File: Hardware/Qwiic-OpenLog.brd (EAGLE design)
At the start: 25.4 x 26.7 mm, 30 parts, among them J2 SMD, J3 PTH, J4 SMD, J5 ISP, Q1 16MHZ, U2 ATMEGA328P, U3 microSD Socket

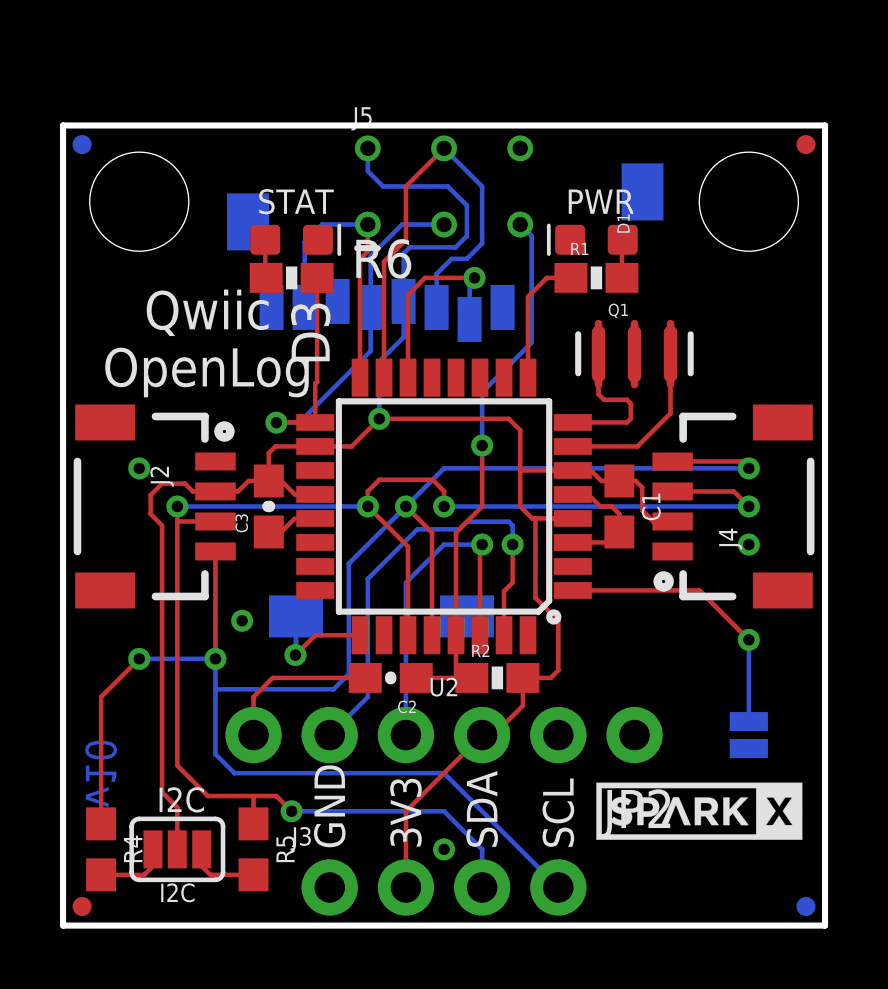
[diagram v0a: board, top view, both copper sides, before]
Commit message: Updating with Buzzard labels
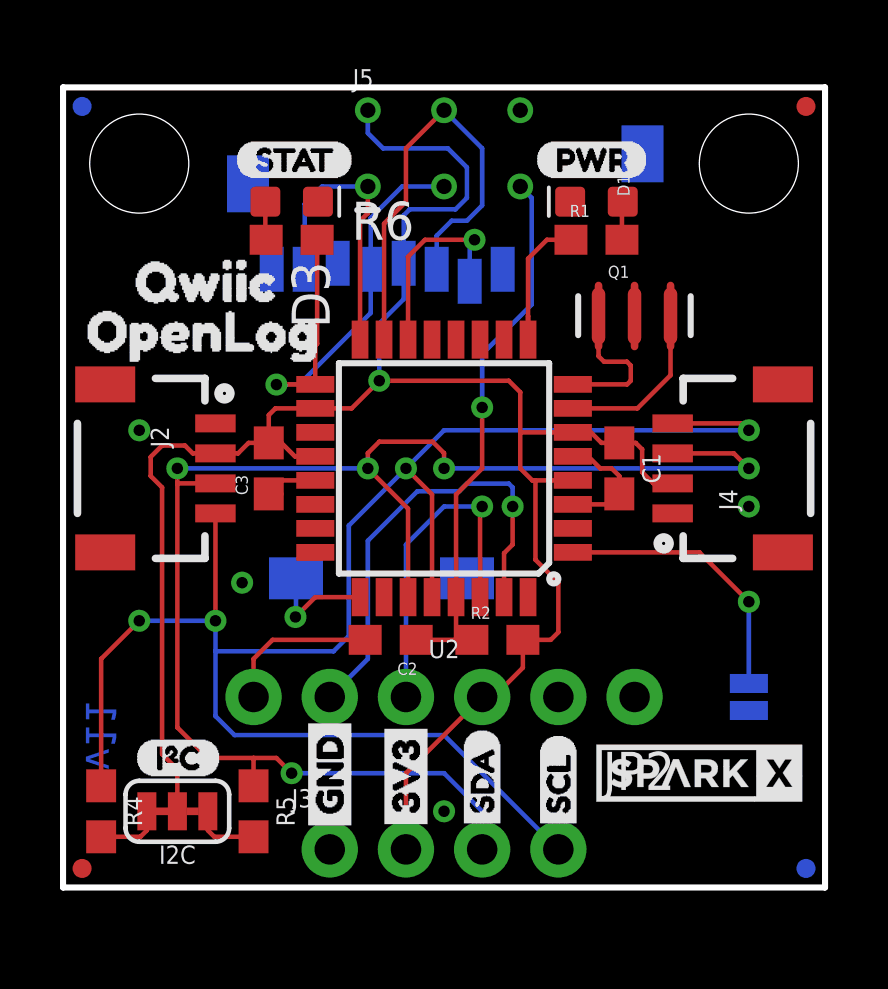
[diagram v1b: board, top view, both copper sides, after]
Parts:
- added U$10: (no value), buzzard_labels (13):BLK3
- added U$11: (no value), buzzard_labels (13):BOOT5
- added U$12: (no value), buzzard_labels (13):GRN4
- added U$13, U$16: (no value), buzzard_labels (13):SDA1
- added U$14: (no value), buzzard_labels (13):QWIIC7
- added U$15, U$19: (no value), buzzard_labels (13):SCL2
- added U$17: (no value), buzzard_labels (13):STAT0
- added U$18: (no value), buzzard_labels (14):OPENLOG0
- added U$20: (no value), buzzard_labels (16):GND1
- added U$4: (no value), Labels:3V3-03
- added U$5: (no value), Labels:GND-03
- added U$6: (no value), buzzard_labels (16):3V30
- added U$7: (no value), Labels:ADR-()-03
- added U$8: (no value), Labels:I_SUPER2_C-()-03
- added U$9: (no value), Labels:PWR-()-03
- C2, C3: device SparkFun-Capacitors:0603-CAP -> SparkFun-Capacitors:0603
- FID1, FID2, FID3, FID4: device SparkFun-Aesthetics:MICRO-FIDUCIAL -> SparkFun-Aesthetics:FIDUCIAL-MICRO
- I2C: value (none) -> JUMPER-SMT_3_2-NC_TRACE_SILK; device SparkFun-Jumpers:SMT-JUMPER_3_2-NC_PASTE_SILK -> SparkFun-Jumpers:SMT-JUMPER_3_2-NC_TRACE_SILK
- R1: value 1K -> 1k; device SparkFun-Resistors:0603-RES -> SparkFun-Resistors:0603
- R2: value 10K -> 10k; device SparkFun-Resistors:0603-RES -> SparkFun-Resistors:0603
- R6: device SparkFun-Resistors:0603-RES -> SparkFun-Resistors:0603
- moved J5 1.27 mm to (12.7, 24.6)
- moved C1 1.27 mm to (18.5, 14.0)
- moved C3 1.27 mm to (6.86, 14.0)
- moved J2 1.27 mm to (5.08, 14.0)
- moved J4 1.27 mm to (20.3, 14.0)
- moved U$1 1.27 mm to (2.54, 14.0)
- moved U2 1.27 mm to (12.7, 14.0)
- moved U3 1.27 mm to (5.71, 9.91)
- moved C2 1.27 mm to (10.9, 8.26)
- moved R2 1.27 mm to (14.5, 8.26)
- moved FID2 1.27 mm to (0.64, 0.64)
- moved FID3 1.27 mm to (24.8, 0.64)
- moved I2C 1.27 mm to (3.81, 2.54)
- moved J3 1.27 mm to (8.89, 1.27)
- moved LOGO2 1.27 mm to (22.9, 2.54)
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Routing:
- net GND: track 4.65 -> 6.27 mm
- net N$1: track 4.01 -> 5.03 mm
- net N$2: track 4.67 -> 5.69 mm
- net N$4: track 4.39 -> 5.18 mm
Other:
- board text added: "v11"
- board text removed: "3V3"
- board text removed: "ADR"
- board text removed: "BLK"
- board text removed: "BOOT"
- board text removed: "GND"
- board text removed: "GRN"
- board text removed: "I2C"
- board text removed: "PWR"
- board text removed: "Qwiic OpenLog"
- board text removed: "SCL"
- board text removed: "SDA"
- board text removed: "STAT"
- board text removed: "v10"

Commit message: Adding pull up on CS pin to allow for easier ISP programming.
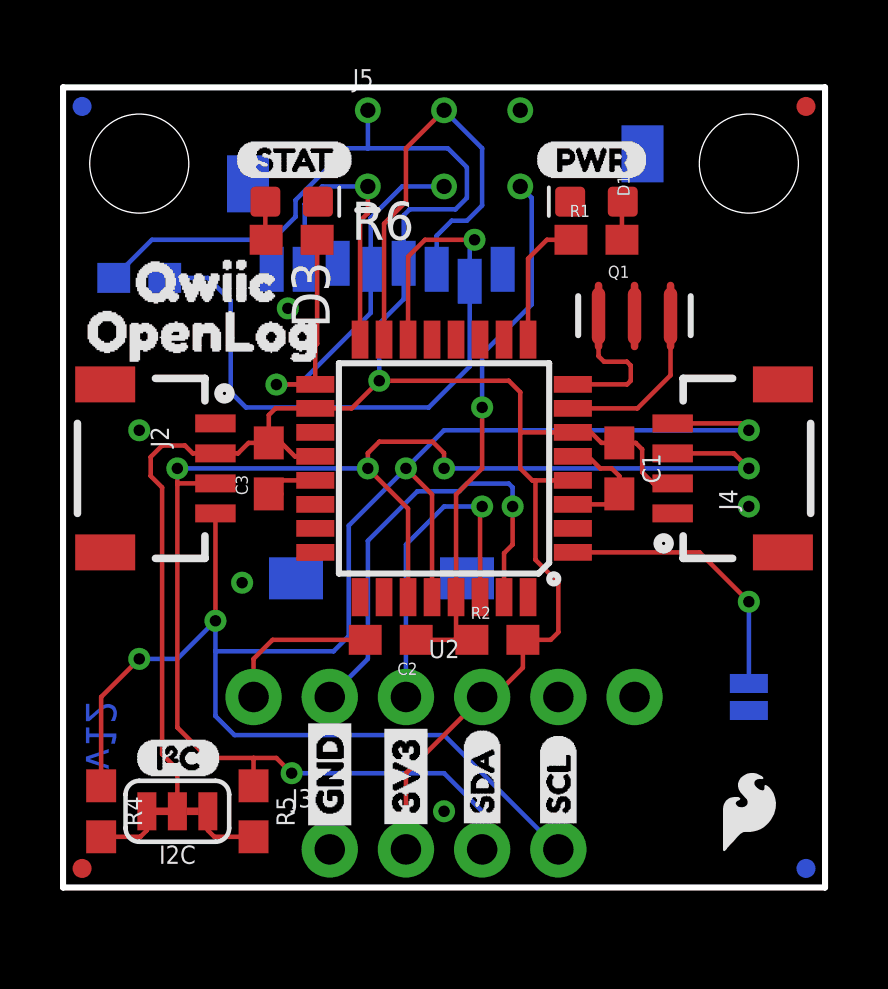
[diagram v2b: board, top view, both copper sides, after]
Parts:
- removed U$1: SPARKX-LOGO4, SparkX:SPARKX-MEDIUM
- removed U$2: SPARKX-LOGO3, SparkX:SPARKX-SMALL
- removed U3: microSD Socket, SparkFun-Connectors:MICRO-SD-SOCKET-PP
- added J1: MICRO-SD, SparkFun-Connectors:MICRO-SD-SOCKET
- added LOGO1: SFE_LOGO_FLAME.1_INCH, SparkFun-Aesthetics:SFE_LOGO_FLAME_.1
- added LOGO4: SFE_LOGO_NAME_FLAME.1_INCH, SparkFun-Aesthetics:SFE_LOGO_NAME_FLAME_.1
- added R3: 10k, SparkFun-Resistors:0603
- added U$3: (no value), Labels:QWIIC-LOGO-SMALL
- I2C: value JUMPER-SMT_3_2-NC_TRACE_SILK -> (none)
- J6: value BOOT -> (none)
- flipped J6 to the bottom, turned to 0 degrees
- renumbered JP2 to J6
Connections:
- removed net CD: U2.25, U3.CD1
- net 3.3V: now also J1.VCC, R3.2; no longer U3.VCC
- net CS: now also J1.CS, R3.1; no longer U3.CS
- net GND: now also J1.GND; no longer U3.GND, U3.GND1, U3.GND3
- net MISO: now also J1.DO; no longer U3.DO
- net MOSI: now also J1.DI; no longer U3.DI
- net SCK: now also J1.SCLK; no longer U3.SCLK
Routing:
- net CS: track 6.66 -> 23.8 mm
- net 3.3V: track 68.1 -> 79.0 mm
- net CD: track 3.72 -> 0.00 mm, vias 1 -> 0
- net N$4: track 5.18 -> 4.39 mm
- net SCL: track 58.9 -> 58.1 mm
- net GND: vias 4 -> 5
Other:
- board text added: "v12"
- board text removed: "v11"
